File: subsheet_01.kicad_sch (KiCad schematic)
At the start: 14 parts, among them J1 JTAG, J3 VPP, U1 ATF1508AS_L_100A_TQFP_JTAG_EN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

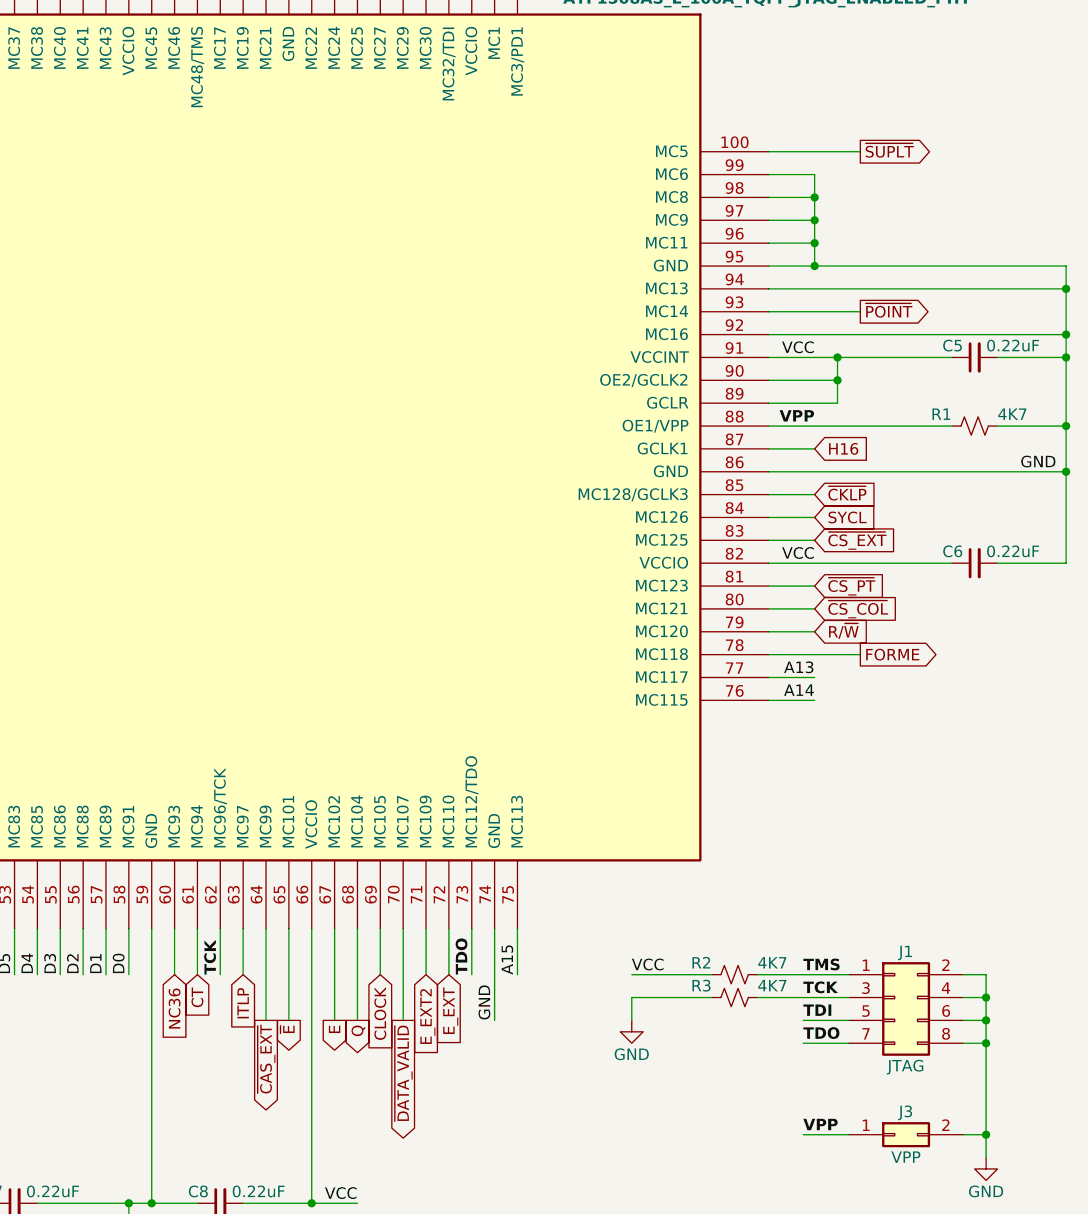
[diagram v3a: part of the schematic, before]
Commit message: pcb/schematics : rework connexion for easier routing, pcb edge, power distribution network
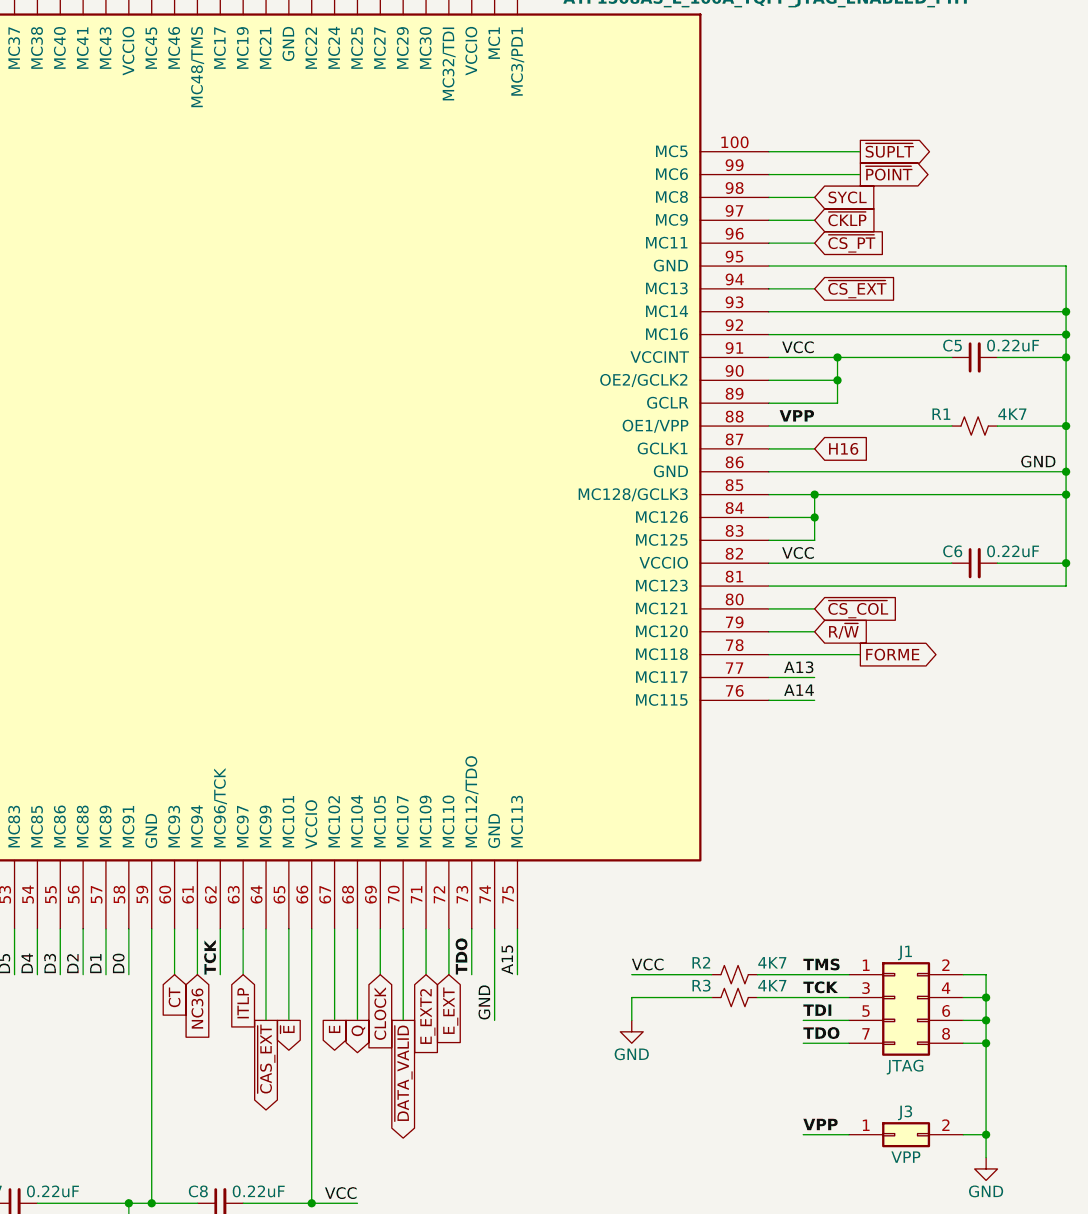
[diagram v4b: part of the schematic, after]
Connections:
- net CT: now also U1.60 (MC93); no longer U1.61 (MC94)
- net GND: now also U1.81 (MC123), U1.83 (MC125), U1.84 (MC126), U1.85 (MC128/GCLK3), U1.93 (MC14); no longer U1.94 (MC13), U1.96 (MC11), U1.97 (MC9), U1.98 (MC8), U1.99 (MC6)
- net NC36: now also U1.61 (MC94); no longer U1.60 (MC93)
- net SYCL: now also U1.98 (MC8); no longer U1.84 (MC126)
- net ~{CKLP}: now also U1.97 (MC9); no longer U1.85 (MC128/GCLK3)
- net ~{CS_EXT}: now also U1.94 (MC13); no longer U1.83 (MC125)
- net ~{CS_PT}: now also U1.96 (MC11); no longer U1.81 (MC123)
- net ~{POINT}: now also U1.99 (MC6); no longer U1.93 (MC14)
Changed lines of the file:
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@@
   (junction (at 20.32 134.62) (diameter 0) (color 0 0 0 0)
   )
-  (junction (at 167.64 119.38) (diameter 0) (color 0 0 0 0)
+  (junction (at 195.58 149.86) (diameter 0) (color 0 0 0 0)
   )
   (junction (at 20.32 147.32) (diameter 0) (color 0 0 0 0)
@@
   (junction (at 186.69 220.98) (diameter 0) (color 0 0 0 0)
   )
+  (junction (at 167.64 152.4) (diameter 0) (color 0 0 0 0)
+  )
+  (junction (at 195.58 129.54) (diameter 0) (color 0 0 0 0)
+  )
   (junction (at 186.69 205.74) (diameter 0) (color 0 0 0 0)
   )
@@
   (junction (at 129.54 63.5) (diameter 0) (color 0 0 0 0)
   )
-  (junction (at 167.64 121.92) (diameter 0) (color 0 0 0 0)
-  )
   (junction (at 195.58 134.62) (diameter 0) (color 0 0 0 0)
   )
@@
   (junction (at 73.66 228.6) (diameter 0) (color 0 0 0 0)
   )
-  (junction (at 195.58 127) (diameter 0) (color 0 0 0 0)
+  (junction (at 167.64 149.86) (diameter 0) (color 0 0 0 0)
   )
   (junction (at 111.76 228.6) (diameter 0) (color 0 0 0 0)
   )
+  (junction (at 195.58 157.48) (diameter 0) (color 0 0 0 0)
+  )
   (junction (at 109.22 81.28) (diameter 0) (color 0 0 0 0)
   )
@@
   (junction (at 170.18 137.16) (diameter 0) (color 0 0 0 0)
   )
-  (junction (at 167.64 124.46) (diameter 0) (color 0 0 0 0)
-  )
-  (junction (at 167.64 116.84) (diameter 0) (color 0 0 0 0)
-  )
   (junction (at 195.58 132.08) (diameter 0) (color 0 0 0 0)
   )
@@
     (stroke (width 0) (type default))
   )
-  (wire (pts (xy 195.58 124.46) (xy 195.58 127))
-    (stroke (width 0) (type default))
-  )
   (wire (pts (xy 20.32 116.84) (xy 20.32 129.54))
     (stroke (width 0) (type default))
@@
     (stroke (width 0) (type default))
   )
-  (wire (pts (xy 167.64 116.84) (xy 167.64 119.38))
-    (stroke (width 0) (type default))
-  )
   (wire (pts (xy 129.54 203.2) (xy 129.54 198.12))
     (stroke (width 0) (type default))
   )
-  (wire (pts (xy 167.64 121.92) (xy 167.64 124.46))
-    (stroke (width 0) (type default))
-  )
   (wire (pts (xy 114.3 81.28) (xy 114.3 88.9))
     (stroke (width 0) (type default))
@@
     (stroke (width 0) (type default))
   )
-  (wire (pts (xy 195.58 147.32) (xy 195.58 157.48))
+  (wire (pts (xy 195.58 147.32) (xy 195.58 149.86))
     (stroke (width 0) (type default))
   )
@@
     (stroke (width 0) (type default))
   )
-  (wire (pts (xy 162.56 160.02) (xy 167.64 160.02))
+  (wire (pts (xy 162.56 160.02) (xy 195.58 160.02))
     (stroke (width 0) (type default))
   )
@@
     (stroke (width 0) (type default))
   )
-  (wire (pts (xy 167.64 119.38) (xy 167.64 121.92))
-    (stroke (width 0) (type default))
-  )
   (wire (pts (xy 99.06 83.82) (xy 99.06 88.9))
     (stroke (width 0) (type default))
@@
     (stroke (width 0) (type default))
   )
-  (wire (pts (xy 162.56 127) (xy 195.58 127))
-    (stroke (width 0) (type default))
-  )
   (wire (pts (xy 109.22 63.5) (xy 116.84 63.5))
     (stroke (width 0) (type default))
@@
     (stroke (width 0) (type default))
   )
+  (wire (pts (xy 167.64 149.86) (xy 195.58 149.86))
+    (stroke (width 0) (type default))
+  )
   (wire (pts (xy 106.68 78.74) (xy 106.68 88.9))
     (stroke (width 0) (type default))
@@
     (stroke (width 0) (type default))
   )
-  (wire (pts (xy 167.64 114.3) (xy 167.64 116.84))
-    (stroke (width 0) (type default))
-  )
   (wire (pts (xy 73.66 88.9) (xy 73.66 83.82))
     (stroke (width 0) (type default))
@@
     (stroke (width 0) (type default))
   )
+  (wire (pts (xy 167.64 152.4) (xy 167.64 154.94))
+    (stroke (width 0) (type default))
+  )
   (wire (pts (xy 162.56 119.38) (xy 167.64 119.38))
     (stroke (width 0) (type default))
@@
     (stroke (width 0) (type default))
   )
-  (wire (pts (xy 195.58 127) (xy 195.58 132.08))
+  (wire (pts (xy 195.58 124.46) (xy 195.58 129.54))
     (stroke (width 0) (type default))
   )
@@
     (stroke (width 0) (type default))
   )
+  (wire (pts (xy 162.56 127) (xy 167.64 127))
+    (stroke (width 0) (type default))
+  )
   (wire (pts (xy 91.44 203.2) (xy 91.44 198.12))
     (stroke (width 0) (type default))
@@
     (stroke (width 0) (type default))
   )
+  (wire (pts (xy 195.58 149.86) (xy 195.58 157.48))
+    (stroke (width 0) (type default))
+  )
   (wire (pts (xy 187.96 142.24) (xy 195.58 142.24))
     (stroke (width 0) (type default))
@@
     (stroke (width 0) (type default))
   )
-  (wire (pts (xy 167.64 124.46) (xy 195.58 124.46))
+  (wire (pts (xy 162.56 124.46) (xy 195.58 124.46))
     (stroke (width 0) (type default))
   )
@@
     (stroke (width 0) (type default))
   )
-  (wire (pts (xy 162.56 129.54) (xy 172.72 129.54))
+  (wire (pts (xy 162.56 129.54) (xy 195.58 129.54))
+    (stroke (width 0) (type default))
+  )
+  (wire (pts (xy 195.58 160.02) (xy 195.58 157.48))
+    (stroke (width 0) (type default))
+  )
+  (wire (pts (xy 195.58 129.54) (xy 195.58 132.08))
     (stroke (width 0) (type default))
   )
@@
     (stroke (width 0) (type default))
   )
-  (wire (pts (xy 162.56 114.3) (xy 167.64 114.3))
+  (wire (pts (xy 162.56 114.3) (xy 172.72 114.3))
     (stroke (width 0) (type default))
   )
@@
     (stroke (width 0) (type default))
   )
+  (wire (pts (xy 167.64 149.86) (xy 167.64 152.4))
+    (stroke (width 0) (type default))
+  )
   (wire (pts (xy 45.72 137.16) (xy 50.8 137.16))
     (stroke (width 0) (type default))
   )
   (wire (pts (xy 162.56 137.16) (xy 170.18 137.16))
-    (stroke (width 0) (type default))
-  )
-  (wire (pts (xy 162.56 124.46) (xy 167.64 124.46))
     (stroke (width 0) (type default))
   )
@@
     )
   )
-  (global_label "~{CS_PT}" (shape input) (at 167.64 160.02 0) (fields_autoplaced)
-    (effects (font (size 1.27 1.27)) (justify left))
-    (property "Intersheetrefs" "${INTERSHEET_REFS}" (at 176.3099 160.02 0)
+  (global_label "~{CS_PT}" (shape input) (at 167.64 121.92 0) (fields_autoplaced)
+    (effects (font (size 1.27 1.27)) (justify left))
+    (property "Intersheetrefs" "${INTERSHEET_REFS}" (at 176.3099 121.92 0)
       (effects (font (size 1.27 1.27)) (justify left) hide)
     )
@@
     )
   )
-  (global_label "~{CKLP}" (shape input) (at 167.64 149.86 0) (fields_autoplaced)
-    (effects (font (size 1.27 1.27)) (justify left))
-    (property "Intersheetrefs" "${INTERSHEET_REFS}" (at 175.4633 149.86 0)
-      (effects (font (size 1.27 1.27)) (justify left) hide)
-    )
-  )
-  (global_label "CT" (shape input) (at 99.06 203.2 270) (fields_autoplaced)
+  (global_label "~{CKLP}" (shape input) (at 167.64 119.38 0) (fields_autoplaced)
+    (effects (font (size 1.27 1.27)) (justify left))
+    (property "Intersheetrefs" "${INTERSHEET_REFS}" (at 175.4633 119.38 0)
+      (effects (font (size 1.27 1.27)) (justify left) hide)
+    )
+  )
+  (global_label "CT" (shape input) (at 96.52 203.2 270) (fields_autoplaced)
     (effects (font (size 1.27 1.27)) (justify right))
-    (property "Intersheetrefs" "${INTERSHEET_REFS}" (at 99.06 208.4228 90)
+    (property "Intersheetrefs" "${INTERSHEET_REFS}" (at 96.52 208.4228 90)
       (effects (font (size 1.27 1.27)) (justify right) hide)
     )
@@
     )
   )
-  (global_label "SYCL" (shape input) (at 167.64 152.4 0) (fields_autoplaced)
-    (effects (font (size 1.27 1.27)) (justify left))
-    (property "Intersheetrefs" "${INTERSHEET_REFS}" (at 175.2214 152.4 0)
+  (global_label "SYCL" (shape input) (at 167.64 116.84 0) (fields_autoplaced)
+    (effects (font (size 1.27 1.27)) (justify left))
+    (property "Intersheetrefs" "${INTERSHEET_REFS}" (at 175.2214 116.84 0)
       (effects (font (size 1.27 1.27)) (justify left) hide)
     )
@@
     )
   )
-  (global_label "~{POINT}" (shape output) (at 172.72 129.54 0) (fields_autoplaced)
-    (effects (font (size 1.27 1.27)) (justify left))
-    (property "Intersheetrefs" "${INTERSHEET_REFS}" (at 181.2086 129.54 0)
-      (effects (font (size 1.27 1.27)) (justify left) hide)
-    )
-  )
-  (global_label "NC36" (shape input) (at 96.52 203.2 270) (fields_autoplaced)
+  (global_label "~{POINT}" (shape output) (at 172.72 114.3 0) (fields_autoplaced)
+    (effects (font (size 1.27 1.27)) (justify left))
+    (property "Intersheetrefs" "${INTERSHEET_REFS}" (at 181.2086 114.3 0)
+      (effects (font (size 1.27 1.27)) (justify left) hide)
+    )
+  )
+  (global_label "NC36" (shape input) (at 99.06 203.2 270) (fields_autoplaced)
     (effects (font (size 1.27 1.27)) (justify right))
-    (property "Intersheetrefs" "${INTERSHEET_REFS}" (at 96.52 211.2047 90)
+    (property "Intersheetrefs" "${INTERSHEET_REFS}" (at 99.06 211.2047 90)
       (effects (font (size 1.27 1.27)) (justify right) hide)
     )
@@
     )
   )
-  (global_label "~{CS_EXT}" (shape input) (at 167.64 154.94 0) (fields_autoplaced)
-    (effects (font (size 1.27 1.27)) (justify left))
-    (property "Intersheetrefs" "${INTERSHEET_REFS}" (at 177.3984 154.94 0)
-      (effects (font (size 1.27 1.27)) (justify left) hide)
-    )
+  (global_label "~{CS_EXT}" (shape input) (at 167.64 127 0) (fields_autoplaced)
+    (effects (font (size 1.27 1.27)) (justify left))
+    (property "Intersheetrefs" "${INTERSHEET_REFS}" (at 177.3984 127 0)
+      (effects (font (size 1.27 1.27)) (justify left) hide)
+    )
